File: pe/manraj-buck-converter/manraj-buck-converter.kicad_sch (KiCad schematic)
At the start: 8 parts, among them U1 AP62300WU-7

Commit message: Added power symbols, net labels, and pwr_flags
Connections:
- net SW: now reaches C2.2, L1.1, U1.2 (SW)
- net FB: now reaches R1.2, R2.1, U1.4 (FB)
- net V_in renamed +12V
- net V_out renamed +5V

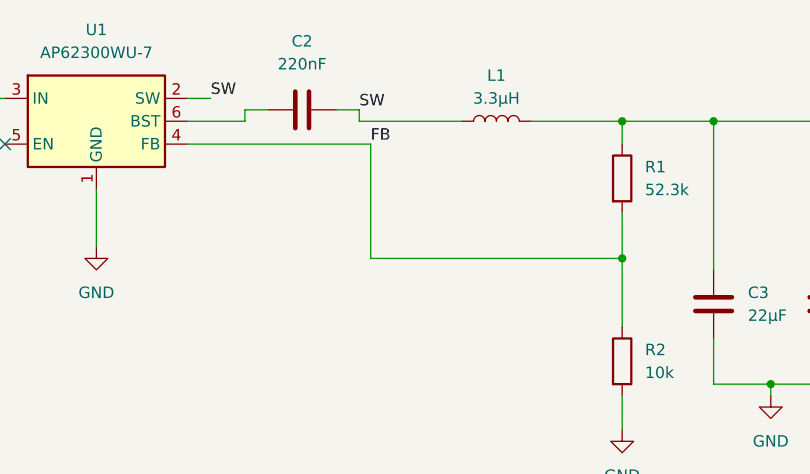
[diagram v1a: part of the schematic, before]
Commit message: Added footprint for SRP7030 Inductor
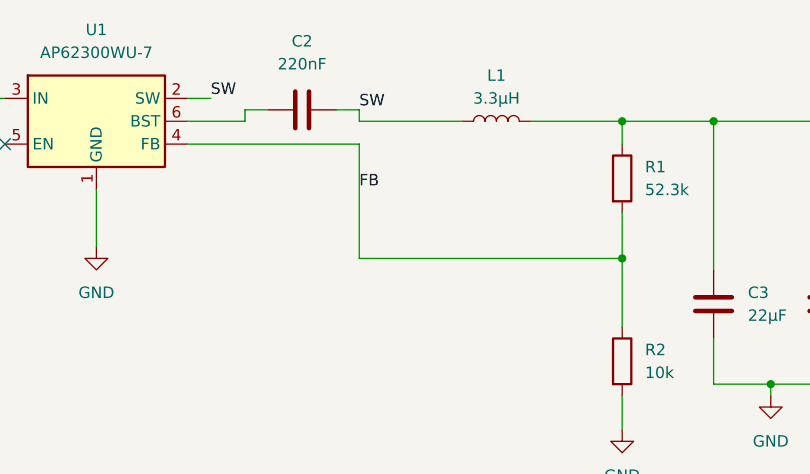
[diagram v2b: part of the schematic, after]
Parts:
- C1, C3, C4: footprint (none) -> Capacitor_SMD:C_1206_3216Metric_Pad1.33x1.80mm_HandSolder
- C2: footprint (none) -> Capacitor_SMD:C_0603_1608Metric_Pad1.08x0.95mm_HandSolder
- L1: footprint Inductor_SMD:L_0201_0603Metric_Pad0.64x0.40mm_HandSolder -> footprints:IND_BOURNS_SRP7030-M
- R1, R2: footprint (none) -> Resistor_SMD:R_0603_1608Metric_Pad0.98x0.95mm_HandSolder
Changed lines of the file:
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@@
-	(wire
-		(pts
-			(xy 162.56 80.01) (xy 162.56 92.71)
-		)
-		(stroke
-			(width 0)
-			(type default)
-		)
-	)
 	(wire
 		(pts
@@
 	(wire
 		(pts
+			(xy 161.29 80.01) (xy 161.29 92.71)
+		)
+		(stroke
+			(width 0)
+			(type default)
+		)
+	)
+	(wire
+		(pts
 			(xy 69.85 74.93) (xy 86.36 74.93)
 		)
@@
 	(wire
 		(pts
-			(xy 142.24 80.01) (xy 162.56 80.01)
-		)
-		(stroke
-			(width 0)
-			(type default)
-		)
-	)
-	(wire
-		(pts
 			(xy 213.36 106.68) (xy 207.01 106.68)
 		)
@@
 	(wire
 		(pts
+			(xy 161.29 80.01) (xy 142.24 80.01)
+		)
+		(stroke
+			(width 0)
+			(type default)
+		)
+	)
+	(wire
+		(pts
 			(xy 190.5 107.95) (xy 190.5 111.76)
 		)
@@
 	(wire
 		(pts
-			(xy 162.56 92.71) (xy 190.5 92.71)
+			(xy 161.29 92.71) (xy 190.5 92.71)
 		)
 		(stroke
@@
 	)
 	(label "FB"
-		(at 162.56 80.01 0)
+		(at 161.29 85.09 0)
 		(effects
 			(font
@@
 			)
 		)
-		(property "Footprint" ""
+		(property "Footprint" "Capacitor_SMD:C_0603_1608Metric_Pad1.08x0.95mm_HandSolder"
 			(at 158.75 75.2348 0)
 			(hide yes)
@@
 			)
 		)
-		(property "Footprint" ""
+		(property "Footprint" "Resistor_SMD:R_0603_1608Metric_Pad0.98x0.95mm_HandSolder"
 			(at 188.722 104.14 90)
 			(hide yes)
@@
 			)
 		)
-		(property "Footprint" "Inductor_SMD:L_0201_0603Metric_Pad0.64x0.40mm_HandSolder"
+		(property "Footprint" "footprints:IND_BOURNS_SRP7030-M"
 			(at 176.53 77.47 0)
 			(hide yes)
@@
 			)
 		)
-		(property "Footprint" ""
+		(property "Footprint" "Capacitor_SMD:C_1206_3216Metric_Pad1.33x1.80mm_HandSolder"
 			(at 201.6252 101.6 0)
 			(hide yes)
@@
 			)
 		)
-		(property "Footprint" ""
+		(property "Footprint" "Resistor_SMD:R_0603_1608Metric_Pad0.98x0.95mm_HandSolder"
 			(at 188.722 83.82 90)
 			(hide yes)
@@
 			)
 		)
-		(property "Footprint" ""
+		(property "Footprint" "Capacitor_SMD:C_1206_3216Metric_Pad1.33x1.80mm_HandSolder"
 			(at 214.3252 101.6 0)
 			(hide yes)
@@
 			)
 		)
-		(property "Footprint" ""
+		(property "Footprint" "Capacitor_SMD:C_1206_3216Metric_Pad1.33x1.80mm_HandSolder"
 			(at 87.3252 99.06 0)
 			(hide yes)

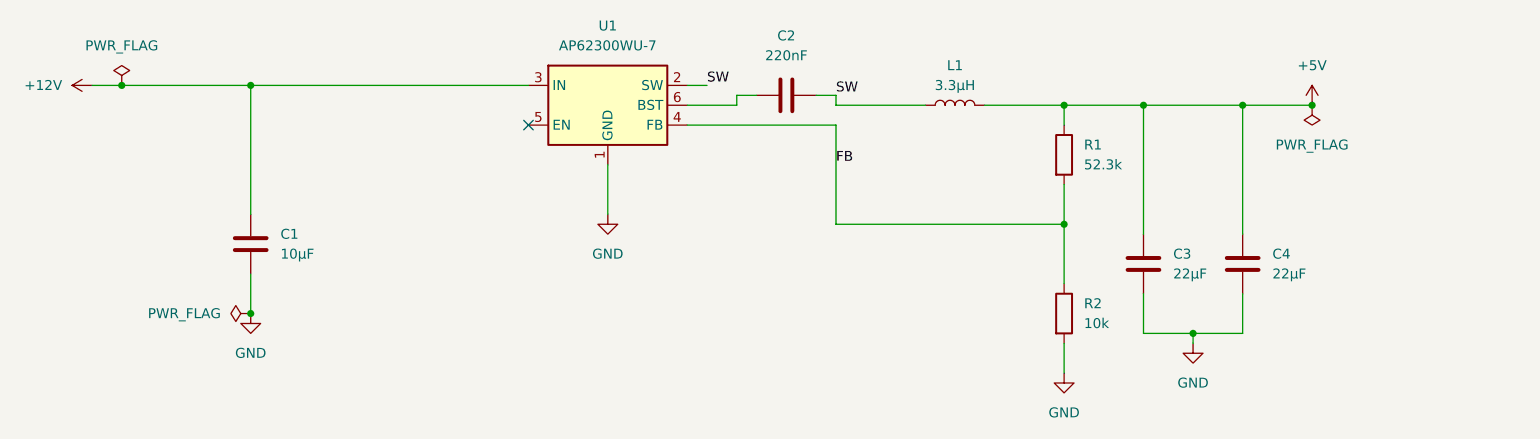
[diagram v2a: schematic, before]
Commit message: Added parallel input capacitors due to DC bias
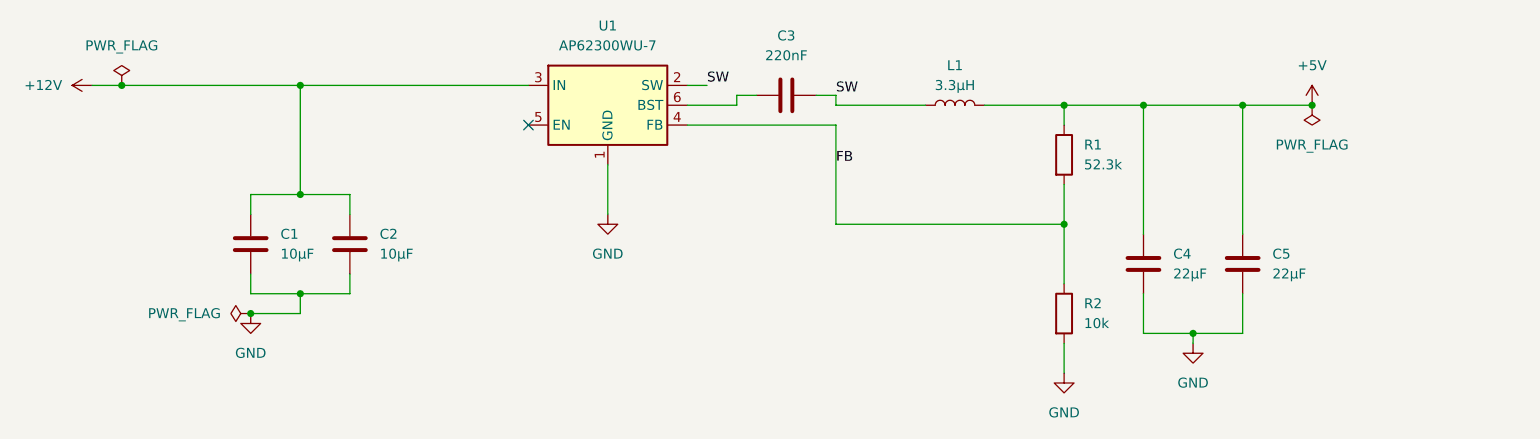
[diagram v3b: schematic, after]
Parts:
- added C2: 10µF, Capacitor_SMD:C_1206_3216Metric_Pad1.33x1.80mm_HandSolder, symbol Device:C
- C1: Digikey Part Number (none) -> 445-180362-1-ND; Digikey URL (none) -> https://www.digikey.com/en/products/detail/tdk/cga5l1x7r1h1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; Manufacturer (none) -> TDK; Manufacturer Part Number (none) -> CGA5L1X7R1H106K160AC
- C3: renamed from C2; Digikey Part Number (none) -> 490-13307-1-ND; Digikey URL (none) -> https://www.digikey.com/en/products/detail/murata-electroni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; Manufacturer (none) -> Murata Electronics; Manufacturer Part Number (none) -> GCM188R71H224KA64J
- L1: footprint footprints:IND_BOURNS_SRP7030-M -> Inductor_SMD:L_Bourns_SRP7028A_7.3x6.6mm; Digikey Part Number (none) -> SRP7028A-3R3MCT-ND; Digikey URL (none) -> https://www.digikey.com/en/products/detail/bourns-inc/srp70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; Manufacturer (none) -> Bourns Inc.; Manufacturer Part Number (none) -> SRP7028A-3R3M
- R1: Digikey Part Number (none) -> P52.3KHCT-ND; Digikey URL (none) -> https://www.digikey.com/en/products/detail/panasonic-indust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; Manufacturer (none) -> Panasonic Industry; Manufacturer Part Number (none) -> ERJ-3EKF5232V
- R2: Digikey Part Number (none) -> P10.0KHCT-ND; Digikey URL (none) -> https://www.digikey.com/en/products/detail/panasonic-indust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; Manufacturer (none) -> Panasonic Industry; Manufacturer Part Number (none) -> ERJ-3EKF1002V
- U1: Digikey Part Number (none) -> 31-AP62300WU-7CT-ND; Digikey URL (none) -> https://www.digikey.com/en/products/detail/diodes-incorpora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; Manufacturer (none) -> Diodes Inc.; Manufacturer Part Number (none) -> AP62300WU-7
- renumbered C3 to C4, C4 to C5
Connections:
- net +12V: now also C2.1
- net GND: now also C2.2

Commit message: Added feed-forward capacitor C6 parallel to R1
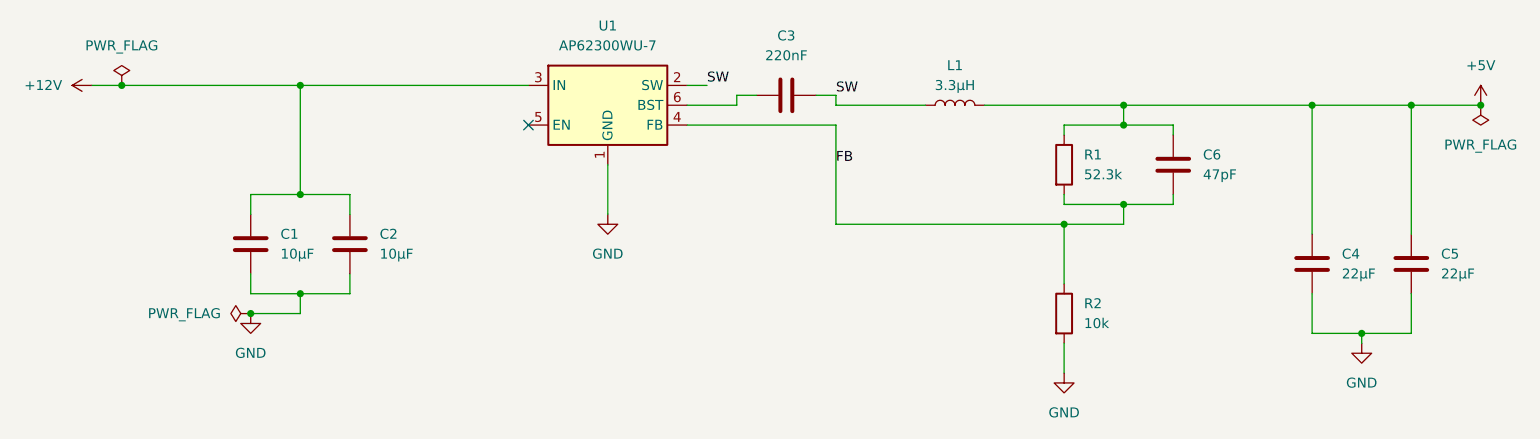
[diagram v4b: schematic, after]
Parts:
- added C6: 47pF, Capacitor_SMD:C_0603_1608Metric_Pad1.08x0.95mm_HandSolder, symbol Device:C
- C4, C5: Digikey Part Number (none) -> 490-GRM31CZ71C226ME15LCT-ND; Digikey URL (none) -> https://www.digikey.com/en/products/detail/murata-electroni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; Manufacturer (none) -> Murata Electronics; Manufacturer Part Number (none) -> GRM31CZ71C226ME15L
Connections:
- net +5V: now also C6.1
- net FB: now also C6.2
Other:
- moved on the sheet: C4, C5, R1
